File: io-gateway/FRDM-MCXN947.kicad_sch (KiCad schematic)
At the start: 1 part

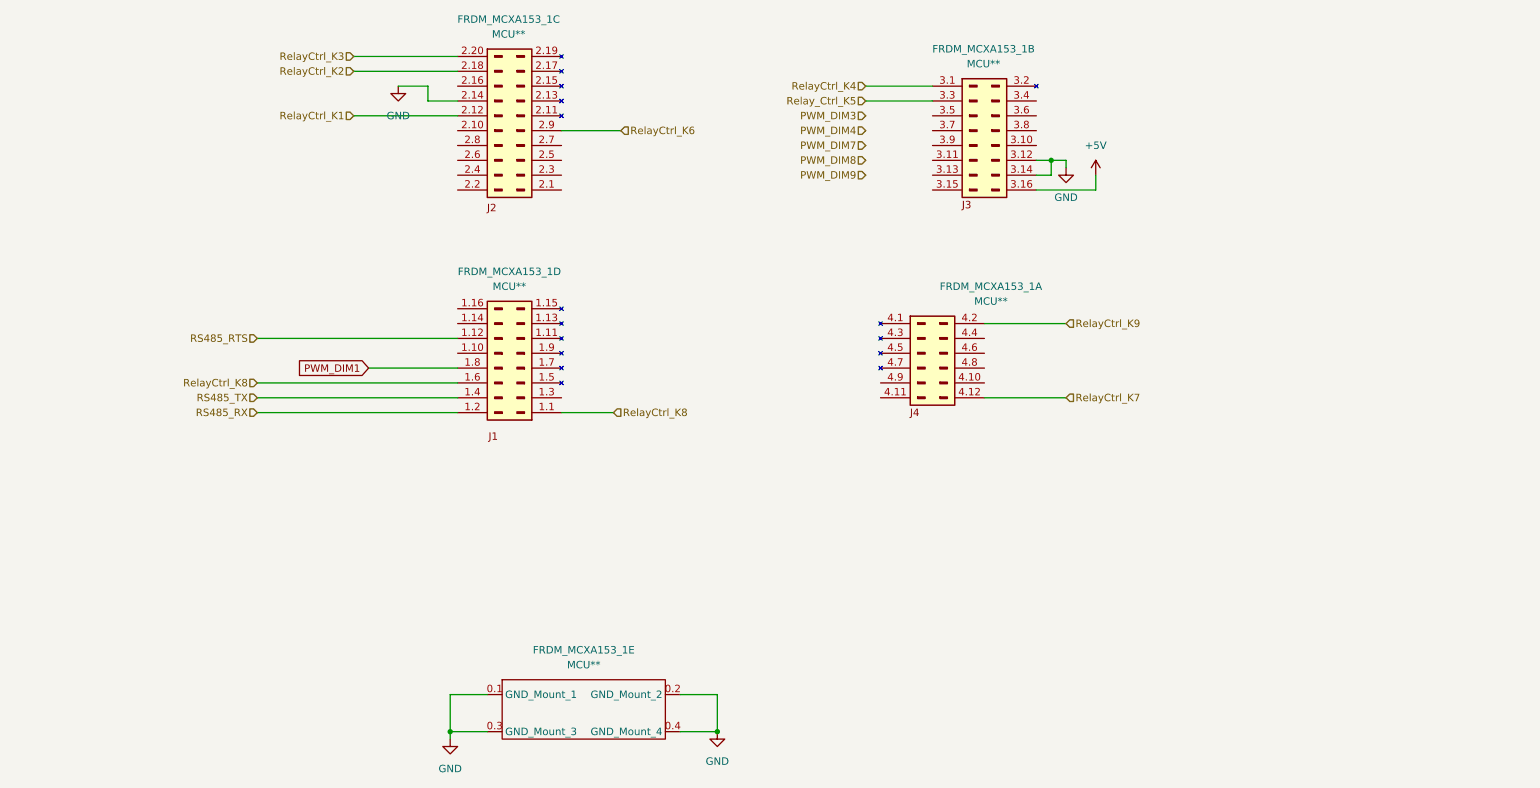
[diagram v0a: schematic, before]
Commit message: add RS485
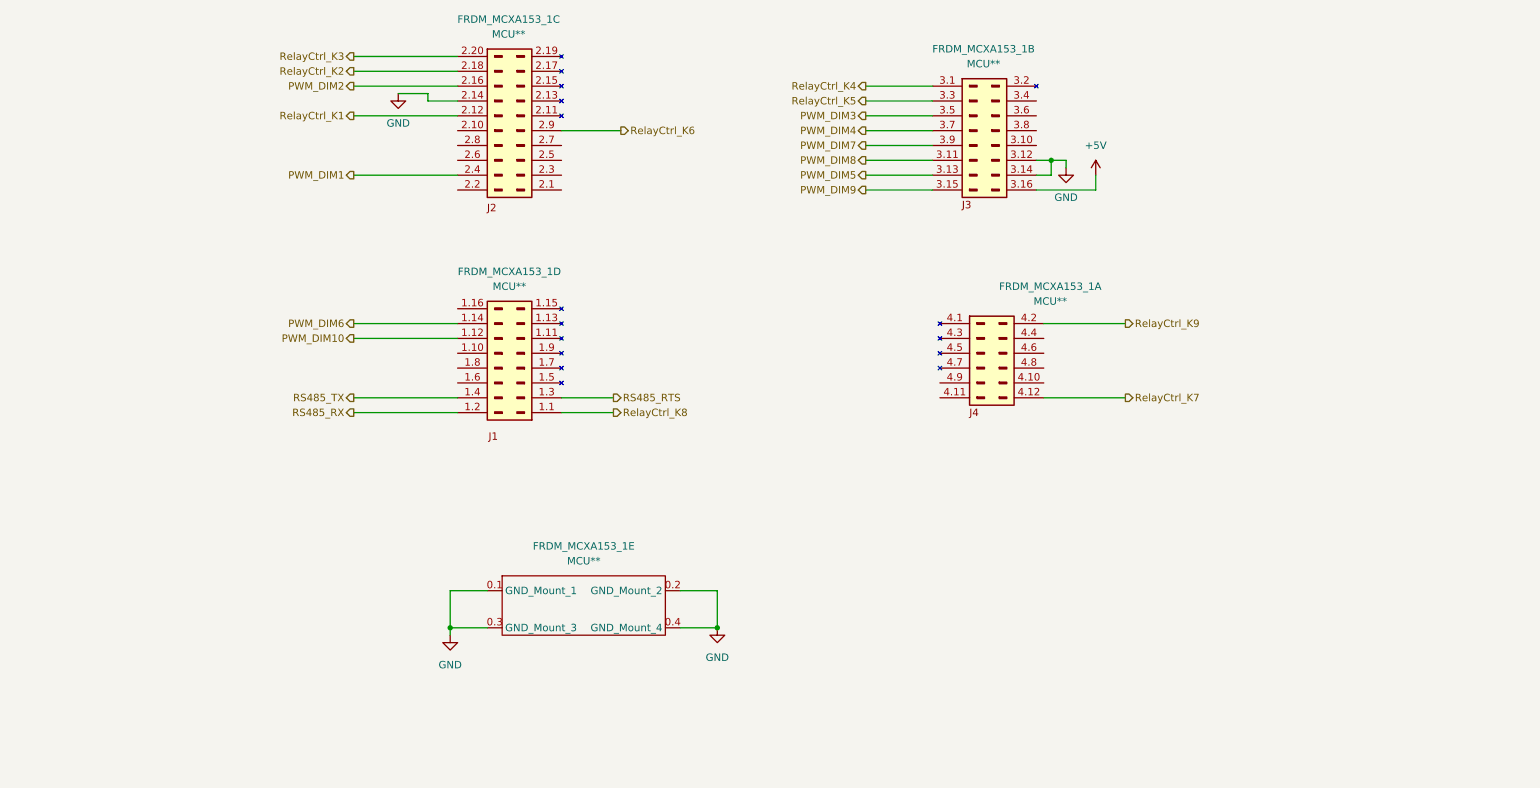
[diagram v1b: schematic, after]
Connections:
- net PWM_DIM1: now also FRDM_MCXA153_1.2.4 (Pin_J2_4); no longer FRDM_MCXA153_1.1.8 (Pin_J1_8)
- net PWM_DIM3: now also FRDM_MCXA153_1.3.5 (Pin_J3_5)
- net PWM_DIM4: now also FRDM_MCXA153_1.3.7 (Pin_J3_7)
- net PWM_DIM7: now also FRDM_MCXA153_1.3.9 (Pin_J3_9)
- net PWM_DIM8: now also FRDM_MCXA153_1.3.11 (Pin_J3_11)
- net PWM_DIM9: now also FRDM_MCXA153_1.3.15 (Pin_J3_15)
- net RS485_RTS: now also FRDM_MCXA153_1.1.3 (Pin_J1_3); no longer FRDM_MCXA153_1.1.12 (Pin_J1_12)
- net RelayCtrl_K8: no longer FRDM_MCXA153_1.1.6 (Pin_J1_6)
- net PWM_DIM6: now reaches FRDM_MCXA153_1.1.14 (Pin_J1_14)
- net PWM_DIM2: now reaches FRDM_MCXA153_1.2.16 (Pin_J2_16)
- net PWM_DIM5: now reaches FRDM_MCXA153_1.3.13 (Pin_J3_13)
- net Relay_Ctrl_K5 renamed RelayCtrl_K5
- new net PWM_DIM10: FRDM_MCXA153_1.1.12 (Pin_J1_12)
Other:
- moved on the sheet: FRDM_MCXA153_1A, FRDM_MCXA153_1E

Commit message: connect all relays
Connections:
- net RelayCtrl_K1: no longer FRDM_MCXA153_1.2.12 (Pin_J2_12)
- net RelayCtrl_K2: now also FRDM_MCXA153_1.4.6 (Pin_6); no longer FRDM_MCXA153_1.2.18 (Pin_J2_18)
- net RelayCtrl_K3: now also FRDM_MCXA153_1.4.2 (Pin_2); no longer FRDM_MCXA153_1.2.20 (Pin_J2_20)
- net RelayCtrl_K6: now also FRDM_MCXA153_1.2.20 (Pin_J2_20); no longer FRDM_MCXA153_1.2.9 (Pin_J2_9)
- net RelayCtrl_K9: now also FRDM_MCXA153_1.4.4 (Pin_4); no longer FRDM_MCXA153_1.4.2 (Pin_2)
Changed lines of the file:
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@@
+	(wire
+		(pts
+			(xy 194.31 120.65) (xy 208.28 120.65)
+		)
+		(stroke
+			(width 0)
+			(type default)
+		)
+	)
 	(wire
 		(pts
@@
 	(wire
 		(pts
+			(xy 76.2 72.39) (xy 93.98 72.39)
+		)
+		(stroke
+			(width 0)
+			(type default)
+		)
+	)
+	(wire
+		(pts
 			(xy 198.12 90.17) (xy 195.58 90.17)
 		)
@@
 	(wire
 		(pts
-			(xy 76.2 72.39) (xy 93.98 72.39)
-		)
-		(stroke
-			(width 0)
-			(type default)
-		)
-	)
-	(wire
-		(pts
 			(xy 99.06 163.83) (xy 92.71 163.83)
 		)
@@
 	(wire
 		(pts
+			(xy 194.31 123.19) (xy 208.28 123.19)
+		)
+		(stroke
+			(width 0)
+			(type default)
+		)
+	)
+	(wire
+		(pts
 			(xy 111.76 133.35) (xy 120.65 133.35)
 		)
@@
 	(wire
 		(pts
-			(xy 111.76 85.09) (xy 121.92 85.09)
-		)
-		(stroke
-			(width 0)
-			(type default)
-		)
-	)
-	(wire
-		(pts
 			(xy 163.83 95.25) (xy 175.26 95.25)
 		)
@@
 	(wire
 		(pts
+			(xy 194.31 118.11) (xy 208.28 118.11)
+		)
+		(stroke
+			(width 0)
+			(type default)
+		)
+	)
+	(wire
+		(pts
 			(xy 76.2 92.71) (xy 93.98 92.71)
 		)
@@
 	(wire
 		(pts
-			(xy 76.2 82.55) (xy 93.98 82.55)
-		)
-		(stroke
-			(width 0)
-			(type default)
-		)
-	)
-	(wire
-		(pts
 			(xy 195.58 92.71) (xy 195.58 90.17)
 		)
@@
 	(wire
 		(pts
-			(xy 194.31 118.11) (xy 208.28 118.11)
-		)
-		(stroke
-			(width 0)
-			(type default)
-		)
-	)
-	(wire
-		(pts
 			(xy 88.9 78.74) (xy 88.9 80.01)
 		)
@@
 	(wire
 		(pts
-			(xy 76.2 74.93) (xy 93.98 74.93)
-		)
-		(stroke
-			(width 0)
-			(type default)
-		)
-	)
-	(wire
-		(pts
 			(xy 76.2 120.65) (xy 93.98 120.65)
 		)
@@
 	(hierarchical_label "RelayCtrl_K1"
 		(shape output)
-		(at 76.2 82.55 180)
-		(effects
-			(font
-				(size 1.27 1.27)
-			)
-			(justify right)
+		(at 119.38 85.09 0)
+		(effects
+			(font
+				(size 1.27 1.27)
+			)
+			(justify left)
 		)
 	)
@@
 	(hierarchical_label "RelayCtrl_K2"
 		(shape output)
-		(at 76.2 74.93 180)
-		(effects
-			(font
-				(size 1.27 1.27)
-			)
-			(justify right)
+		(at 208.28 123.19 0)
+		(effects
+			(font
+				(size 1.27 1.27)
+			)
+			(justify left)
 		)
 	)
@@
 	(hierarchical_label "RelayCtrl_K6"
 		(shape output)
-		(at 121.92 85.09 0)
-		(effects
-			(font
-				(size 1.27 1.27)
-			)
-			(justify left)
+		(at 76.2 72.39 180)
+		(effects
+			(font
+				(size 1.27 1.27)
+			)
+			(justify right)
 		)
 	)
@@
 	(hierarchical_label "RelayCtrl_K9"
 		(shape output)
+		(at 208.28 120.65 0)
+		(effects
+			(font
+				(size 1.27 1.27)
+			)
+			(justify left)
+		)
+	)
+	(hierarchical_label "PWM_DIM6"
+		(shape output)
+		(at 76.2 118.11 180)
+		(effects
+			(font
+				(size 1.27 1.27)
+			)
+			(justify right)
+		)
+	)
+	(hierarchical_label "RS485_TX"
+		(shape output)
+		(at 76.2 130.81 180)
+		(effects
+			(font
+				(size 1.27 1.27)
+			)
+			(justify right)
+		)
+	)
+	(hierarchical_label "PWM_DIM8"
+		(shape output)
+		(at 163.83 90.17 180)
+		(effects
+			(font
+				(size 1.27 1.27)
+			)
+			(justify right)
+		)
+	)
+	(hierarchical_label "RelayCtrl_K3"
+		(shape output)
 		(at 208.28 118.11 0)
 		(effects
@@
 		)
 	)
-	(hierarchical_label "PWM_DIM6"
-		(shape output)
-		(at 76.2 118.11 180)
-		(effects
-			(font
-				(size 1.27 1.27)
-			)
-			(justify right)
-		)
-	)
-	(hierarchical_label "RS485_TX"
-		(shape output)
-		(at 76.2 130.81 180)
-		(effects
-			(font
-				(size 1.27 1.27)
-			)
-			(justify right)
-		)
-	)
-	(hierarchical_label "PWM_DIM8"
-		(shape output)
-		(at 163.83 90.17 180)
-		(effects
-			(font
-				(size 1.27 1.27)
-			)
-			(justify right)
-		)
-	)
-	(hierarchical_label "RelayCtrl_K3"
-		(shape output)
-		(at 76.2 72.39 180)
-		(effects
-			(font
-				(size 1.27 1.27)
-			)
-			(justify right)
-		)
-	)

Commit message: connect inh pins
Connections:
- net RelayCtrl_K1: now also FRDM_MCXA153_1.2.18 (Pin_J2_18)
- net INH_DIM_7u8: now reaches FRDM_MCXA153_1.4.11 (Pin_11)
- net INH_DIM_9u10: now reaches FRDM_MCXA153_1.4.8 (Pin_8)
- net INH_DIM_3u4: now reaches FRDM_MCXA153_1.4.9 (Pin_9)
- net INH_DIM_5u6: now reaches FRDM_MCXA153_1.2.2 (Pin_J2_2)
- net ADC_IN2: now reaches FRDM_MCXA153_1.2.7 (Pin_J2_7)
- net INH_DIM_1u2: now reaches FRDM_MCXA153_1.2.9 (Pin_J2_9)
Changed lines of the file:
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@@
+	(wire
+		(pts
+			(xy 111.76 85.09) (xy 120.65 85.09)
+		)
+		(stroke
+			(width 0)
+			(type default)
+		)
+	)
 	(wire
 		(pts
@@
 	(wire
 		(pts
+			(xy 166.37 128.27) (xy 176.53 128.27)
+		)
+		(stroke
+			(width 0)
+			(type default)
+		)
+	)
+	(wire
+		(pts
 			(xy 132.08 163.83) (xy 138.43 163.83)
 		)
@@
 	(wire
 		(pts
+			(xy 76.2 95.25) (xy 93.98 95.25)
+		)
+		(stroke
+			(width 0)
+			(type default)
+		)
+	)
+	(wire
+		(pts
+			(xy 111.76 87.63) (xy 120.65 87.63)
+		)
+		(stroke
+			(width 0)
+			(type default)
+		)
+	)
+	(wire
+		(pts
 			(xy 203.2 92.71) (xy 203.2 95.25)
 		)
@@
 	(wire
 		(pts
+			(xy 166.37 130.81) (xy 176.53 130.81)
+		)
+		(stroke
+			(width 0)
+			(type default)
+		)
+	)
+	(wire
+		(pts
+			(xy 194.31 125.73) (xy 208.28 125.73)
+		)
+		(stroke
+			(width 0)
+			(type default)
+		)
+	)
+	(wire
+		(pts
 			(xy 76.2 120.65) (xy 93.98 120.65)
 		)
@@
 	(wire
 		(pts
+			(xy 76.2 74.93) (xy 93.98 74.93)
+		)
+		(stroke
+			(width 0)
+			(type default)
+		)
+	)
+	(wire
+		(pts
 			(xy 132.08 170.18) (xy 138.43 170.18)
 		)
@@
 	(hierarchical_label "RelayCtrl_K1"
 		(shape output)
-		(at 119.38 85.09 0)
-		(effects
-			(font
-				(size 1.27 1.27)
-			)
-			(justify left)
+		(at 76.2 74.93 180)
+		(effects
+			(font
+				(size 1.27 1.27)
+			)
+			(justify right)
 		)
 	)
@@
 		)
 	)
+	(hierarchical_label "ADC_IN2"
+		(shape input)
+		(at 120.65 87.63 0)
+		(effects
+			(font
+				(size 1.27 1.27)
+			)
+			(justify left)
+		)
+	)
 	(hierarchical_label "RelayCtrl_K2"
 		(shape output)
@@
 		)
 	)
+	(hierarchical_label "INH_DIM_7u8"
+		(shape output)
+		(at 166.37 130.81 180)
+		(effects
+			(font
+				(size 1.27 1.27)
+			)
+			(justify right)
+		)
+	)
 	(hierarchical_label "RelayCtrl_K5"
 		(shape output)
@@
 		)
 	)
+	(hierarchical_label "INH_DIM_1u2"
+		(shape output)
+		(at 120.65 85.09 0)
+		(effects
+			(font
+				(size 1.27 1.27)
+			)
+			(justify left)
+		)
+	)
 	(hierarchical_label "RS485_TX"
 		(shape output)
@@
 		)
 	)
+	(hierarchical_label "ADC_IN1"
+		(shape input)
+		(at 127 97.79 0)
+		(effects
+			(font
+				(size 1.27 1.27)
+			)
+			(justify left)
+		)
+	)
 	(hierarchical_label "RelayCtrl_K4"
 		(shape output)
@@
 		)
 	)
+	(hierarchical_label "INH_DIM_3u4"
+		(shape output)
+		(at 166.37 128.27 180)
+		(effects
+			(font
+				(size 1.27 1.27)
+			)
+			(justify right)
+		)
+	)
 	(hierarchical_label "RS485_RX"
-		(shape output)
+		(shape input)
 		(at 76.2 133.35 180)
 		(effects
@@
 		)
 	)
+	(hierarchical_label "INH_DIM_5u6"
+		(shape output)
+		(at 76.2 95.25 180)
+		(effects
+			(font
+				(size 1.27 1.27)
+			)
+			(justify right)
+		)
+	)
 	(hierarchical_label "PWM_DIM1"
 		(shape output)
@@
 		)
 	)
+	(hierarchical_label "INH_DIM_9u10"
+		(shape output)
+		(at 208.28 125.73 0)
+		(effects
+			(font
+				(size 1.27 1.27)
+			)
+			(justify left)
+		)
+	)

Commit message: upd
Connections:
- net PWM_DIM3 is gone; now on net PWM_DIM2: FRDM_MCXA153_1.3.5 (Pin_J3_5)
- net PWM_DIM4 is gone; now on net PWM_DIM7: FRDM_MCXA153_1.3.7 (Pin_J3_7)
- net INH_DIM_1u2: now also FRDM_MCXA153_1.2.2 (Pin_J2_2); no longer FRDM_MCXA153_1.2.9 (Pin_J2_9)
- net INH_DIM_5u6: now also FRDM_MCXA153_1.2.9 (Pin_J2_9); no longer FRDM_MCXA153_1.2.2 (Pin_J2_2)
- net PWM_DIM2: no longer FRDM_MCXA153_1.2.16 (Pin_J2_16)
- net PWM_DIM7: no longer FRDM_MCXA153_1.3.9 (Pin_J3_9)
- net PWM_DIM8: now also FRDM_MCXA153_1.3.9 (Pin_J3_9); no longer FRDM_MCXA153_1.3.11 (Pin_J3_11)
- net RelayCtrl_K1: now also FRDM_MCXA153_1.4.6 (Pin_6); no longer FRDM_MCXA153_1.2.18 (Pin_J2_18)
- net RelayCtrl_K2: now also FRDM_MCXA153_1.2.20 (Pin_J2_20); no longer FRDM_MCXA153_1.4.6 (Pin_6)
- net RelayCtrl_K3: now also FRDM_MCXA153_1.2.18 (Pin_J2_18); no longer FRDM_MCXA153_1.4.2 (Pin_2)
- net RelayCtrl_K6: now also FRDM_MCXA153_1.4.2 (Pin_2); no longer FRDM_MCXA153_1.2.20 (Pin_J2_20)

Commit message: upd
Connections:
- net INH_DIM_7u8: now also FRDM_MCXA153_1.3.11 (Pin_J3_11); no longer FRDM_MCXA153_1.4.11 (Pin_11)
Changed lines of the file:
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@@
+	(wire
+		(pts
+			(xy 163.83 90.17) (xy 175.26 90.17)
+		)
+		(stroke
+			(width 0)
+			(type default)
+		)
+	)
 	(wire
 		(pts
@@
 		(pts
 			(xy 163.83 82.55) (xy 175.26 82.55)
-		)
-		(stroke
-			(width 0)
-			(type default)
-		)
-	)
-	(wire
-		(pts
-			(xy 166.37 130.81) (xy 176.53 130.81)
 		)
 		(stroke
@@
 	(hierarchical_label "INH_DIM_7u8"
 		(shape output)
-		(at 166.37 130.81 180)
-		(effects
-			(font
+		(at 163.83 90.17 180)
+		(effects
+			(font

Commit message: upd
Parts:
- added C9: 100nF, Capacitor_SMD:C_0603_1608Metric, symbol Device:C
- added D_F1: MMSD914, Diode_SMD:D_SOD-123, symbol Diode:MMSD914
- added M1: Fan_3pin, Connector:FanPinHeader_1x03_P2.54mm_Vertical, symbol Motor:Fan_3pin
- added Q_F1: NTR4003NT1G, Package_TO_SOT_SMD:SOT-23-3, symbol NTR4003NT1G:NTR4003NT1G
- added R_F1: 100, Resistor_SMD:R_0603_1608Metric, symbol Device:R
- added U6: MCP9700x-ETT, Package_TO_SOT_SMD:SOT-23, symbol Sensor_Temperature:MCP9700x-ETT
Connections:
- net +5V: now also C9.1, U6.1 (V_{DD})
- net GND: now also C9.2, Q_F1.2 (S), U6.3 (GND)
- net at FRDM_MCXA153_1.1.10 (Pin_J1_10): now also M1.3 (Tacho)
- net at FRDM_MCXA153_1.1.8 (Pin_J1_8): now also R_F1.2
- net TEMP_VOUT: now reaches FRDM_MCXA153_1.4.10 (Pin_10)
- net TEMP_VOUT: now also U6.2 (V_{OUT})
- new net: Q_F1.1 (G), R_F1.1
- new net: D_F1.2 (A), M1.1 (-), Q_F1.3 (D)
- new net +24V: D_F1.1 (K), M1.2 (+)

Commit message: gen gerbers
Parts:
- added C10, C11: C, Capacitor_SMD:C_0603_1608Metric, symbol Device:C
- added R3, R4: R, Resistor_SMD:R_0603_1608Metric, symbol Device:R
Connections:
- net ADC_IN1: now also R4.2
- net ADC_IN2: now also R3.2; no longer FRDM_MCXA153_1.2.7 (Pin_J2_7)
- net GND: now also C10.2, C11.2
- net INH_DIM_9u10: now also FRDM_MCXA153_1.4.11 (Pin_11); no longer FRDM_MCXA153_1.4.8 (Pin_8)
- net TEMP_VOUT: now also FRDM_MCXA153_1.4.8 (Pin_8); no longer FRDM_MCXA153_1.4.10 (Pin_10)
- net UART1_RTS: now reaches FRDM_MCXA153_1.2.10 (Pin_J2_10)
- net UART1_RX: now reaches FRDM_MCXA153_1.2.12 (Pin_J2_12)
- net at FRDM_MCXA153_1.2.5 (Pin_J2_5): now also C10.1, R4.1
- net GPIO1: now reaches FRDM_MCXA153_1.2.6 (Pin_J2_6)
- net UART1_TX: now reaches FRDM_MCXA153_1.2.8 (Pin_J2_8)
- net INH_DIM_3u4: no longer names the net of FRDM_MCXA153_1.4.9 (Pin_9)
- new net: C11.1, FRDM_MCXA153_1.2.7 (Pin_J2_7), R3.1
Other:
- moved on the sheet: C9, FRDM_MCXA153_1B, U6

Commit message: fix minor issues
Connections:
- net GPIO1: no longer names the net of FRDM_MCXA153_1.2.6 (Pin_J2_6)
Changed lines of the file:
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@@
-	(wire
-		(pts
-			(xy 76.2 90.17) (xy 93.98 90.17)
-		)
-		(stroke
-			(width 0)
-			(type default)
-		)
-	)
 	(wire
 		(pts
@@
 		(effects
 			(font
-				(size 1.27 1.27)
-			)
-			(justify right)
-		)
-	)
-	(hierarchical_label "GPIO1"
-		(shape input)
-		(at 76.2 90.17 180)
-		(effects
-			(font
